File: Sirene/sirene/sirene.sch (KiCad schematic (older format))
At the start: 19 parts, among them Q1 BC557, Q2 BC547, Q3 BC557, Q4 BC557, Q5 TIP42

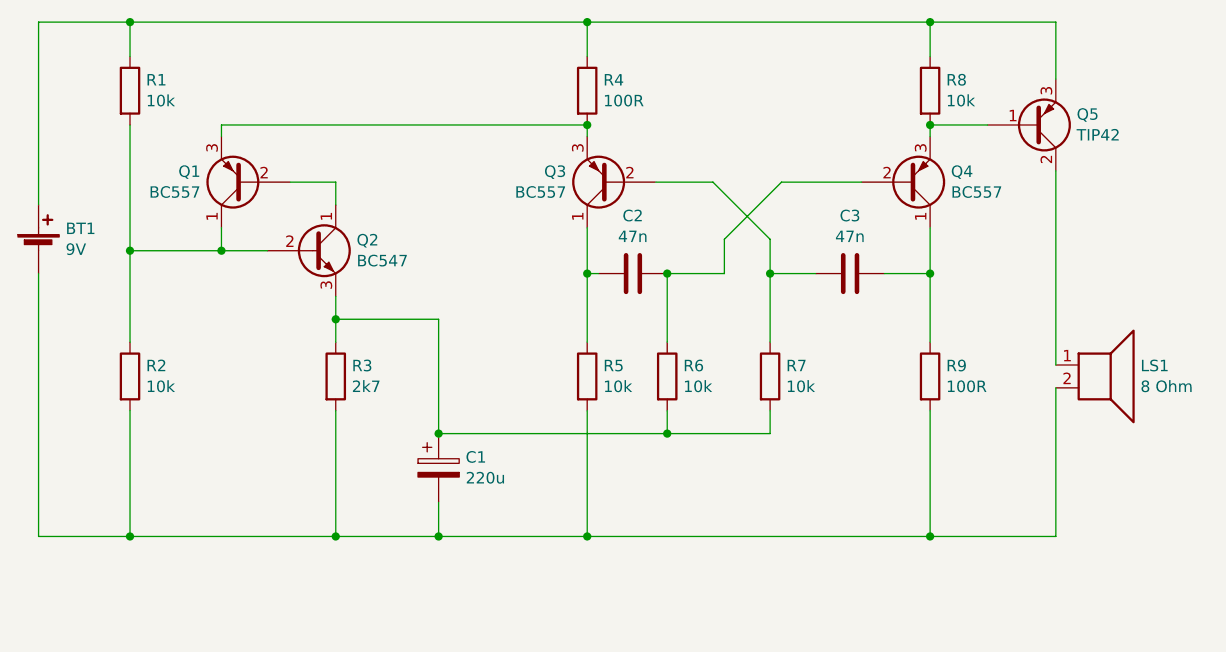
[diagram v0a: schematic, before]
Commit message: Sirene PCB layout.
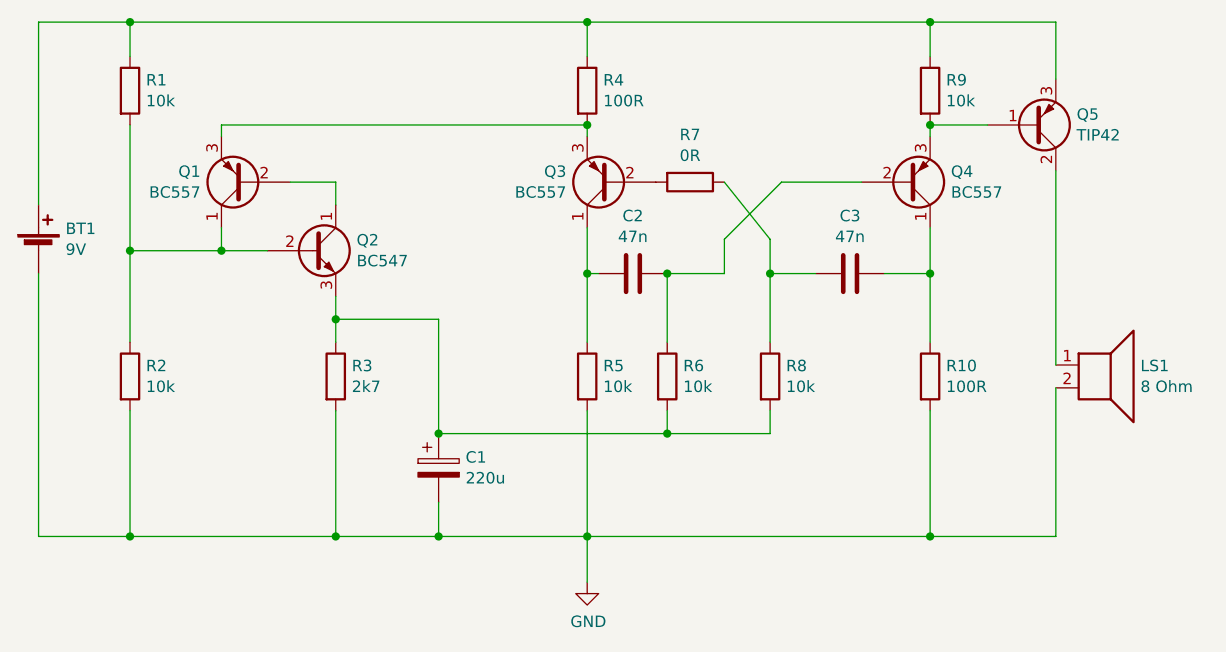
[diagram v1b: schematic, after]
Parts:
- added R7: 0R, Resistor_THT:R_Axial_DIN0207_L6.3mm_D2.5mm_P7.62mm_Horizontal, symbol Device:R
- renumbered R9 to R10, R7 to R8, R8 to R9
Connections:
- net GND: now reaches BT1.2 (-), C1.2, LS1.2, R10.2, R2.2, R3.2, R5.2
- net at C3.2, R8.1: now also R7.1; no longer Q3.2 (B)
- new net: Q3.2 (B), R7.2
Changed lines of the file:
@@
 EESchema Schematic File Version 4
+LIBS:sirene-cache
 EELAYER 30 0
 EELAYER END
@@
 Connection ~ 5350 4050
 $Comp
-L Device:R R7
+L Device:R R8
 U 1 1 5EE575F3
 P 6800 3800
-F 0 "R7" H 6870 3846 50  0000 L CNN
+F 0 "R8" H 6870 3846 50  0000 L CNN
 F 1 "10k" H 6870 3755 50  0000 L CNN
 F 2 "Resistor_THT:R_Axial_DIN0207_L6.3mm_D2.5mm_P7.62mm_Horizontal" V 6730 3800 50  0001 C CNN
@@
 	6800 3200 6800 3350
 Wire Wire Line
-	6550 2950 6800 3200
+	6600 2950 6800 3200
 $Comp
 L Device:C C3
@@
 	6800 3350 6800 3650
 $Comp
-L Device:R R9
+L Device:R R10
 U 1 1 5EE5A8F4
 P 7500 3800
-F 0 "R9" H 7570 3846 50  0000 L CNN
+F 0 "R10" H 7570 3846 50  0000 L CNN
 F 1 "100R" H 7570 3755 50  0000 L CNN
 F 2 "Resistor_THT:R_Axial_DIN0207_L6.3mm_D2.5mm_P7.62mm_Horizontal" V 7430 3800 50  0001 C CNN
@@
 Connection ~ 7500 3350
 $Comp
-L Device:R R8
+L Device:R R9
 U 1 1 5EE66064
 P 7500 2550
-F 0 "R8" H 7570 2596 50  0000 L CNN
+F 0 "R9" H 7570 2596 50  0000 L CNN
 F 1 "10k" H 7570 2505 50  0000 L CNN
 F 2 "Resistor_THT:R_Axial_DIN0207_L6.3mm_D2.5mm_P7.62mm_Horizontal" V 7430 2550 50  0001 C CNN
@@
 Connection ~ 6000 2700
 Wire Wire Line
-	6550 2950 6300 2950
-Wire Wire Line
 	6850 2950 7200 2950
 Wire Wire Line
@@
 Wire Wire Line
 	6350 3350 6600 3350
+$Comp
+L power:GND #PWR01
+U 1 1 5EE4CE5A
+P 6000 4700
+F 0 "#PWR01" H 6000 4450 50  0001 C CNN
+F 1 "GND" H 6005 4527 50  0000 C CNN
+F 2 "" H 6000 4700 50  0001 C CNN
+F 3 "" H 6000 4700 50  0001 C CNN
+	1    6000 4700
+	1    0    0    -1
+$EndComp
+Wire Wire Line
+	6000 4700 6000 4500
+$Comp
+L Device:R R7
+U 1 1 5EE4EEDE
+P 6450 2950
+F 0 "R7" V 6243 2950 50  0000 C CNN
+F 1 "0R" V 6334 2950 50  0000 C CNN
+F 2 "Resistor_THT:R_Axial_DIN0207_L6.3mm_D2.5mm_P7.62mm_Horizontal" V 6380 2950 50  0001 C CNN
+F 3 "~" H 6450 2950 50  0001 C CNN
+	1    6450 2950
+	0    1    1    0
+$EndComp
 $EndSCHEMATC
